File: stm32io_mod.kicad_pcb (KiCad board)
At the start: 2 copper layers, 70.5 x 73.7 mm, 53 parts, among them J1 UART, M1 BluePill, Q1 BC858, Q2 BC858, Q3 BC858, Q4 BC858, SW1 button_1, SW2 button_2, SW3 button_3, SW4 button_4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

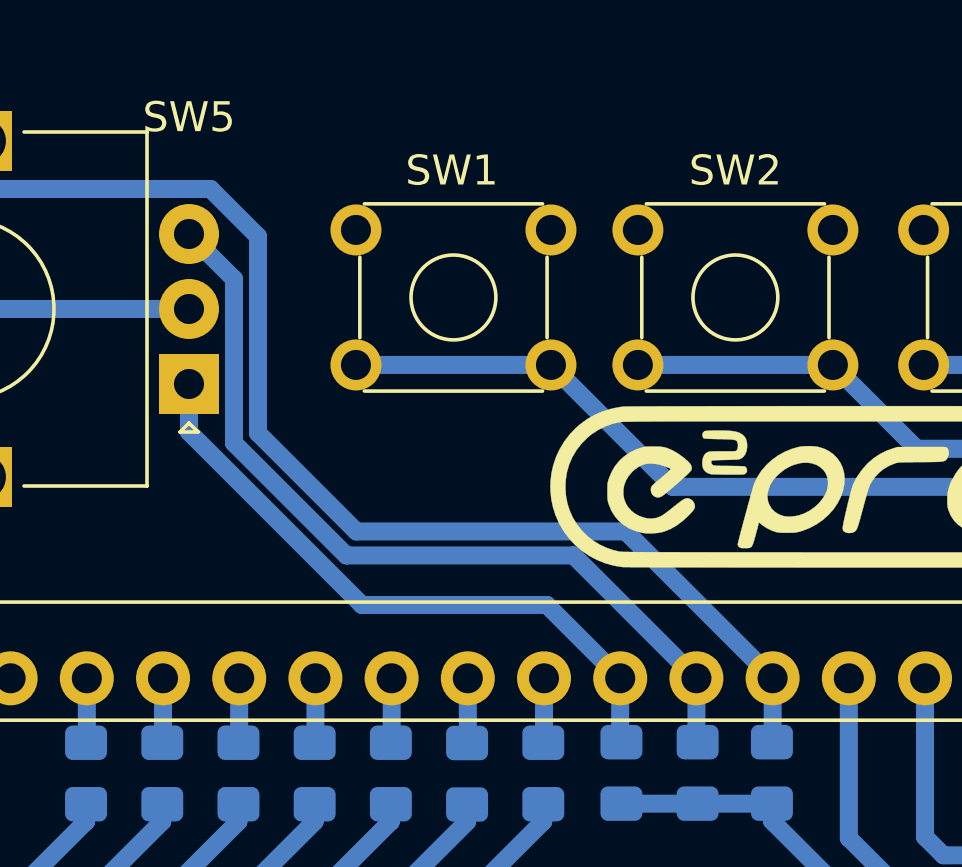
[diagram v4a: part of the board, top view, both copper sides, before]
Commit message: Se agregó una linea de gnd entre el rotary
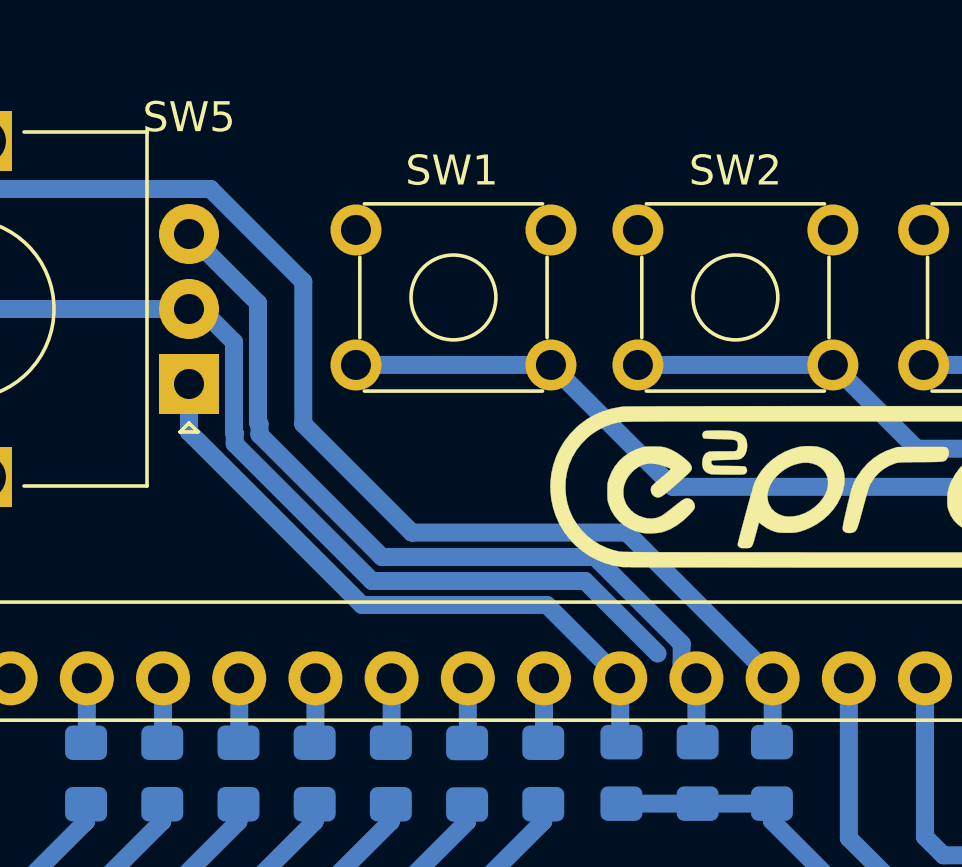
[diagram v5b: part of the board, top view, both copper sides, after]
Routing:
- net GND: track 15.5 -> 37.9 mm
- net swr: track 47.3 -> 46.3 mm
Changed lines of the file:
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@@
     (thickness 1.6)
     (drawings 7)
-    (tracks 287)
+    (tracks 299)
     (zones 0)
     (modules 53)
@@
   (segment (start 120.842 69.382) (end 118.342 71.882) (width 0.6) (layer B.Cu) (net 9))
   (segment (start 132.842 69.382) (end 120.842 69.382) (width 0.6) (layer B.Cu) (net 9))
+  (segment (start 138.939374 78.44799) (end 146.043992 78.44799) (width 0.6) (layer B.Cu) (net 9))
+  (segment (start 134.366 73.874616) (end 138.939374 78.44799) (width 0.6) (layer B.Cu) (net 9))
+  (segment (start 134.366 73.517498) (end 134.366 73.874616) (width 0.6) (layer B.Cu) (net 9))
+  (segment (start 134.342001 73.493499) (end 134.366 73.517498) (width 0.6) (layer B.Cu) (net 9))
+  (segment (start 134.342001 70.481999) (end 134.342001 73.493499) (width 0.6) (layer B.Cu) (net 9))
+  (segment (start 133.242002 69.382) (end 134.342001 70.481999) (width 0.6) (layer B.Cu) (net 9))
+  (segment (start 146.043992 78.44799) (end 148.463 80.866998) (width 0.6) (layer B.Cu) (net 9))
+  (segment (start 132.842 69.382) (end 133.242002 69.382) (width 0.6) (layer B.Cu) (net 9))
   (segment (start 114.180659 96.210419) (end 114.180659 119.171359) (width 0.6) (layer B.Cu) (net 10))
   (segment (start 118.7412 123.7319) (end 120.2412 123.7319) (width 0.6) (layer B.Cu) (net 10))
@@
   (segment (start 147.216 83.7795) (end 147.2565 83.82) (width 0.6) (layer B.Cu) (net 42))
   (segment (start 147.216 81.692) (end 147.216 83.7795) (width 0.6) (layer B.Cu) (net 42))
-  (segment (start 134.342001 68.382001) (end 134.342001 73.850617) (width 0.6) (layer B.Cu) (net 43))
-  (segment (start 134.342001 73.850617) (end 138.088384 77.597) (width 0.6) (layer B.Cu) (net 43))
-  (segment (start 132.842 66.882) (end 134.342001 68.382001) (width 0.6) (layer B.Cu) (net 43))
   (segment (start 149.733 81.669) (end 149.756 81.692) (width 0.6) (layer B.Cu) (net 43))
-  (segment (start 145.661 77.597) (end 149.756 81.692) (width 0.6) (layer B.Cu) (net 43))
-  (segment (start 138.088384 77.597) (end 145.661 77.597) (width 0.6) (layer B.Cu) (net 43))
   (segment (start 149.756 83.7795) (end 149.7965 83.82) (width 0.6) (layer B.Cu) (net 43))
   (segment (start 149.756 81.692) (end 149.756 83.7795) (width 0.6) (layer B.Cu) (net 43))
-  (segment (start 135.142011 73.519243) (end 138.419758 76.79699) (width 0.6) (layer B.Cu) (net 44))
-  (segment (start 135.142011 66.962009) (end 135.142011 73.519243) (width 0.6) (layer B.Cu) (net 44))
-  (segment (start 133.562001 65.381999) (end 135.142011 66.962009) (width 0.6) (layer B.Cu) (net 44))
-  (segment (start 119.842001 65.381999) (end 133.562001 65.381999) (width 0.6) (layer B.Cu) (net 44))
-  (segment (start 118.342 66.882) (end 119.842001 65.381999) (width 0.6) (layer B.Cu) (net 44))
+  (segment (start 149.263008 80.535622) (end 149.263008 81.199008) (width 0.6) (layer B.Cu) (net 43))
+  (segment (start 146.375366 77.64798) (end 149.263008 80.535622) (width 0.6) (layer B.Cu) (net 43))
+  (segment (start 139.270748 77.64798) (end 146.375366 77.64798) (width 0.6) (layer B.Cu) (net 43))
+  (segment (start 135.1915 73.568732) (end 139.270748 77.64798) (width 0.6) (layer B.Cu) (net 43))
+  (segment (start 135.1915 73.211614) (end 135.1915 73.568732) (width 0.6) (layer B.Cu) (net 43))
+  (segment (start 135.142011 69.182011) (end 135.142011 73.162125) (width 0.6) (layer B.Cu) (net 43))
+  (segment (start 149.263008 81.199008) (end 149.756 81.692) (width 0.6) (layer B.Cu) (net 43))
+  (segment (start 135.142011 73.162125) (end 135.1915 73.211614) (width 0.6) (layer B.Cu) (net 43))
+  (segment (start 132.842 66.882) (end 135.142011 69.182011) (width 0.6) (layer B.Cu) (net 43))
   (segment (start 152.273 81.669) (end 152.296 81.692) (width 0.6) (layer B.Cu) (net 44))
-  (segment (start 147.40099 76.79699) (end 152.296 81.692) (width 0.6) (layer B.Cu) (net 44))
-  (segment (start 138.419758 76.79699) (end 147.40099 76.79699) (width 0.6) (layer B.Cu) (net 44))
   (segment (start 152.296 83.797) (end 152.273 83.82) (width 0.6) (layer B.Cu) (net 44))
   (segment (start 152.296 81.692) (end 152.296 83.797) (width 0.6) (layer B.Cu) (net 44))
+  (segment (start 133.562001 65.381999) (end 136.652 68.471998) (width 0.6) (layer B.Cu) (net 44))
+  (segment (start 119.842001 65.381999) (end 133.562001 65.381999) (width 0.6) (layer B.Cu) (net 44))
+  (segment (start 118.342 66.882) (end 119.842001 65.381999) (width 0.6) (layer B.Cu) (net 44))
+  (segment (start 136.652 68.471998) (end 136.652 73.2155) (width 0.6) (layer B.Cu) (net 44))
+  (segment (start 136.652 73.2155) (end 140.2715 76.835) (width 0.6) (layer B.Cu) (net 44))
+  (segment (start 147.439 76.835) (end 152.296 81.692) (width 0.6) (layer B.Cu) (net 44))
+  (segment (start 140.2715 76.835) (end 147.439 76.835) (width 0.6) (layer B.Cu) (net 44))
   (segment (start 144.907 71.247) (end 138.407 71.247) (width 0.6) (layer B.Cu) (net 45))
   (segment (start 162.456 83.707) (end 162.56 83.811) (width 0.6) (layer B.Cu) (net 45))

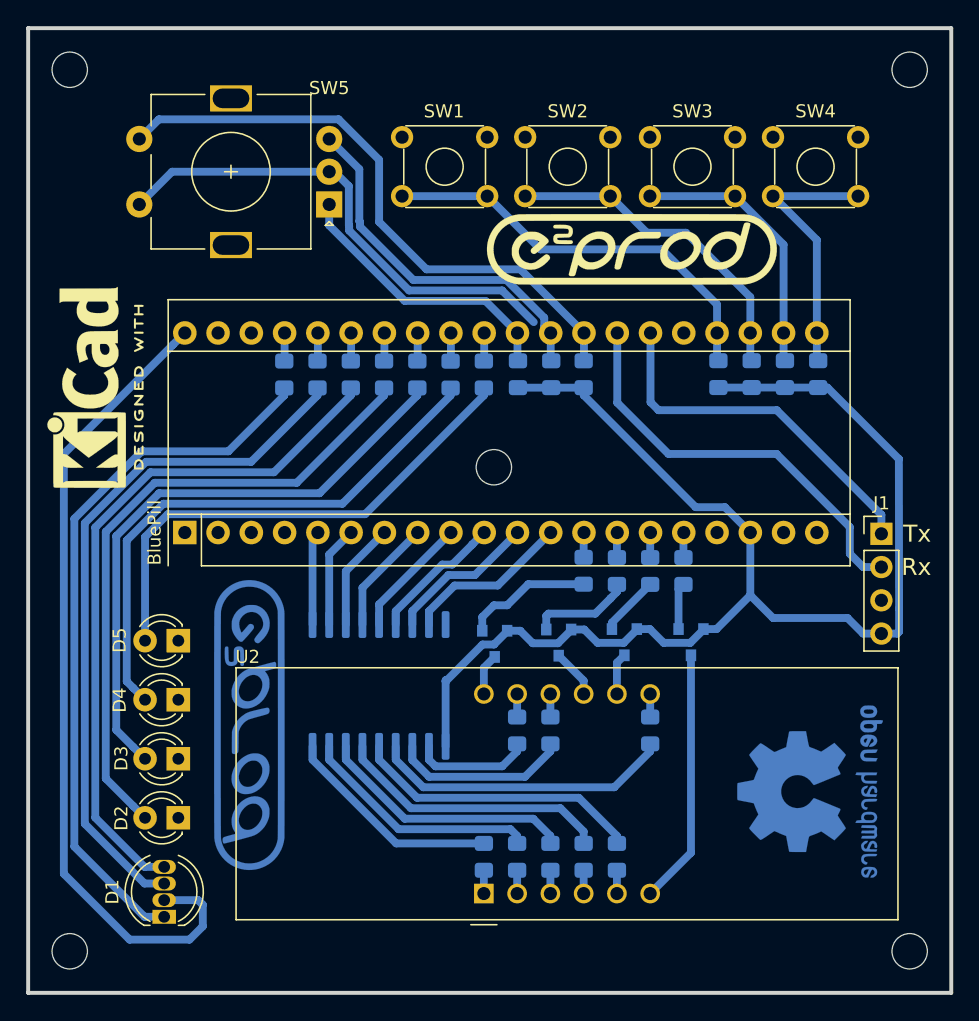
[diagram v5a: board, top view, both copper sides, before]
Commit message: Cambio de polaridad de los LEDs 2-5
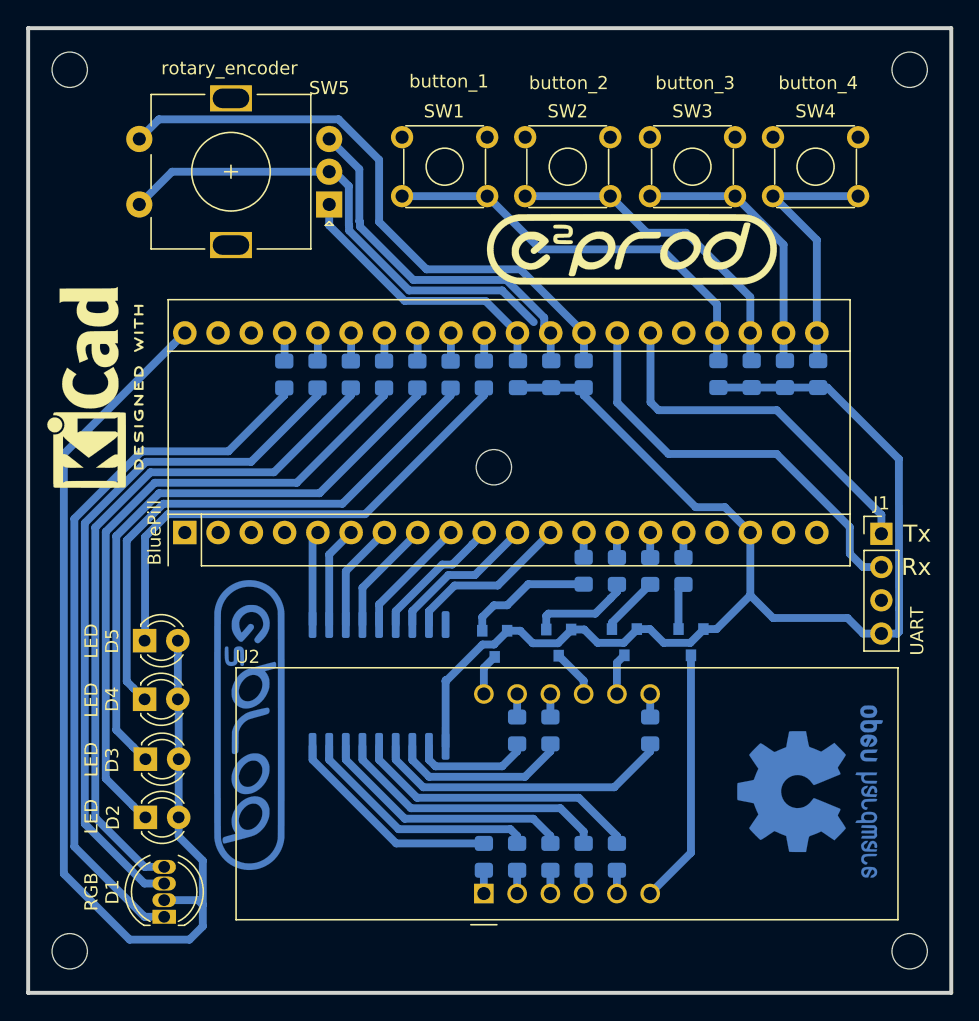
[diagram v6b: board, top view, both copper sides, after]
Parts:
- moved D4 2.58 mm to (118.7, 109.7), turned to 0 degrees
- moved D5 2.58 mm to (118.7, 105.2), turned to 0 degrees
- moved D2 2.51 mm to (118.8, 118.7), turned to 0 degrees
- moved D3 2.51 mm to (118.8, 114.2), turned to 0 degrees
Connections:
- D2 pad 1: GND -> Net-(D2-Pad1)
- D2 pad 2: Net-(D2-Pad2) -> VCC
- D3 pad 1: GND -> Net-(D3-Pad1)
- D3 pad 2: Net-(D3-Pad2) -> VCC
- D4 pad 1: GND -> Net-(D4-Pad1)
- D4 pad 2: Net-(D4-Pad2) -> VCC
- D5 pad 1: GND -> Net-(D5-Pad1)
- D5 pad 2: Net-(D5-Pad2) -> VCC
- R22 pad 1: Net-(D2-Pad2) -> Net-(D2-Pad1)
- R23 pad 1: Net-(D3-Pad2) -> Net-(D3-Pad1)
- R24 pad 1: Net-(D4-Pad2) -> Net-(D4-Pad1)
- R25 pad 1: Net-(D5-Pad2) -> Net-(D5-Pad1)
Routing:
- net Net-(D2-Pad2): track 49.2 -> 0.00 mm
- net Net-(D2-Pad1): track 0.00 -> 49.2 mm
- net Net-(D3-Pad2): track 45.9 -> 0.00 mm
- net Net-(D3-Pad1): track 0.00 -> 45.9 mm
- net Net-(D4-Pad2): track 42.6 -> 0.00 mm
- net Net-(D4-Pad1): track 0.00 -> 42.6 mm
- net Net-(D5-Pad1): track 0.00 -> 38.9 mm
- net Net-(D5-Pad2): track 38.8 -> 0.00 mm
- net VCC: track 166.1 -> 187.0 mm

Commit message: Corrección en la serigrafía de la bluepill y UART
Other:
- board text added: "3v3"
- board text added: "GND"

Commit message: ....
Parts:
- removed the REF** at (177.2, 128.9)
- removed the REF** at (145.4, 91.9)
- removed the REF** at (177.2, 61.6)
- removed the REF** at (113.0, 61.6)
- removed the REF** at (113.0, 128.9)
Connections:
- M1 pad 1: Net-(M1-Pad1) -> (no net)
- M1 pad 17: Net-(M1-Pad17) -> (no net)
- M1 pad 2: Net-(M1-Pad2) -> (no net)
- M1 pad 25: Net-(M1-Pad25) -> (no net)
- M1 pad 28: swr -> led4
- M1 pad 29: rotB -> swr
- M1 pad 3: Net-(M1-Pad3) -> (no net)
- M1 pad 30: rotA -> rotB
- M1 pad 31: led4 -> rotA
- M1 pad 38: Net-(M1-Pad38) -> (no net)
- M1 pad 4: Net-(M1-Pad4) -> (no net)
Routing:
- net led4: track 2.19 -> 18.8 mm, vias 0 -> 2
- net GND: track 37.9 -> 53.2 mm, vias 0 -> 2
- net VCC: track 187.0 -> 188.5 mm
- net rotB: track 28.2 -> 27.1 mm
- net rotA: track 21.6 -> 20.8 mm
- net swr: track 46.3 -> 45.7 mm
